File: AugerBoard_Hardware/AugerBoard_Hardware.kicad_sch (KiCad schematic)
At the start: 44 parts, among them J1 RJ45_LED_Shielded, J2 Conn_01x04_MountingPin, Q1 BSS138, Q2 BSS138, Q3 BSS138, SW1 SW_SPDT, SW2 SW_Push, SW3 SW_Push, SW4 SW_Push, U1 Teensy4.1_DEV-16771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

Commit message: Layout fun time yippie #based #awesome
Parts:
- J2: footprint Connector_PinHeader_2.54mm:PinHeader_1x04_P2.54mm_Horizontal -> Connector_PinHeader_2.54mm:PinHeader_1x04_P2.54mm_Vertical
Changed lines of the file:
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@@
 			)
 		)
-		(property "Footprint" "Connector_PinHeader_2.54mm:PinHeader_1x04_P2.54mm_Horizontal"
+		(property "Footprint" "Connector_PinHeader_2.54mm:PinHeader_1x04_P2.54mm_Vertical"
 			(at 180.34 160.02 0)
 			(effects

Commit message: Layout made smaller hai
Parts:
- Conn10, Conn11, Conn4, Conn5: footprint MRDT_Connectors:MOLEX_SL_02_Horizontal -> MRDT_Connectors:MOLEX_SL_02_Vertical
- Conn13, Conn15, Conn9: footprint MRDT_Connectors:MOLEX_SL_05_Horizontal -> MRDT_Connectors:MOLEX_SL_05_Vertical
- Conn2, Conn3: footprint MRDT_Connectors:MOLEX_SL_04_Horizontal -> MRDT_Connectors:MOLEX_SL_04_Vertical
- Conn7: footprint MRDT_Connectors:MOLEX_SL_03_Horizontal -> MRDT_Connectors:MOLEX_SL_03_Vertical
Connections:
- net +3.3V: now also U1.3.3V_1 (3.3V), U1.3.3V_2 (3.3V), U1.3.3V_3 (3.3V)
- no-connect marks 23 -> 22
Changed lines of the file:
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@@
 	)
 	(no_connect
-		(at 265.43 31.75)
-	)
-	(no_connect
 		(at 265.43 34.29)
 	)
@@
 	(wire
 		(pts
+			(xy 273.05 31.75) (xy 265.43 31.75)
+		)
+		(stroke
+			(width 0)
+			(type default)
+		)
+	)
+	(wire
+		(pts
 			(xy 127 170.18) (xy 132.08 170.18)
 		)
@@
 	(wire
 		(pts
+			(xy 273.05 26.67) (xy 273.05 31.75)
+		)
+		(stroke
+			(width 0)
+			(type default)
+		)
+	)
+	(wire
+		(pts
 			(xy 351.79 196.85) (xy 351.79 199.39)
 		)
@@
 	)
 	(symbol
+		(lib_id "power:+3.3V")
+		(at 273.05 26.67 0)
+		(unit 1)
+		(exclude_from_sim no)
+		(in_bom yes)
+		(on_board yes)
+		(dnp no)
+		(fields_autoplaced yes)
+		(property "Reference" "#PWR014"
+			(at 273.05 30.48 0)
+			(effects
+				(font
+					(size 1.27 1.27)
+				)
+				(hide yes)
+			)
+		)
+		(property "Value" "+3.3V"
+			(at 273.05 21.59 0)
+			(effects
+				(font
+					(size 1.27 1.27)
+				)
+			)
+		)
+		(property "Footprint" ""
+			(at 273.05 26.67 0)
+			(effects
+				(font
+					(size 1.27 1.27)
+				)
+				(hide yes)
+			)
+		)
+		(property "Datasheet" ""
+			(at 273.05 26.67 0)
+			(effects
+				(font
+					(size 1.27 1.27)
+				)
+				(hide yes)
+			)
+		)
+		(property "Description" "Power symbol creates a global label with name \"+3.3V\""
+			(at 273.05 26.67 0)
+			(effects
+				(font
+					(size 1.27 1.27)
+				)
+				(hide yes)
+			)
+		)
+		(pin "1"
+		)
+		(instances
+			(project ""
+				(path "/eb675789-6cce-4465-8b28-94d3d6dee9aa"
+					(reference "#PWR014")
+					(unit 1)
+				)
+			)
+		)
+	)
+	(symbol
 		(lib_id "Switch:SW_Push")
 		(at 111.76 93.98 0)
@@
 			)
 		)
-		(property "Footprint" "MRDT_Connectors:MOLEX_SL_04_Horizontal"
+		(property "Footprint" "MRDT_Connectors:MOLEX_SL_04_Vertical"
 			(at 167.64 36.83 0)
 			(effects
@@
 			)
 		)
-		(property "Footprint" "MRDT_Connectors:MOLEX_SL_02_Horizontal"
+		(property "Footprint" "MRDT_Connectors:MOLEX_SL_02_Vertical"
 			(at 67.31 132.08 0)
 			(effects
@@
 			)
 		)
-		(property "Footprint" "MRDT_Connectors:MOLEX_SL_03_Horizontal"
+		(property "Footprint" "MRDT_Connectors:MOLEX_SL_03_Vertical"
 			(at 231.14 167.64 0)
 			(effects
@@
 			)
 		)
-		(property "Footprint" "MRDT_Connectors:MOLEX_SL_04_Horizontal"
+		(property "Footprint" "MRDT_Connectors:MOLEX_SL_04_Vertical"
 			(at 167.64 59.69 0)
 			(effects
@@
 			)
 		)
-		(property "Footprint" "MRDT_Connectors:MOLEX_SL_02_Horizontal"
+		(property "Footprint" "MRDT_Connectors:MOLEX_SL_02_Vertical"
 			(at 67.31 104.14 0)
 			(effects
@@
 			)
 		)
-		(property "Footprint" "MRDT_Connectors:MOLEX_SL_05_Horizontal"
+		(property "Footprint" "MRDT_Connectors:MOLEX_SL_05_Vertical"
 			(at 387.35 118.11 0)
 			(effects
@@
 			)
 		)
-		(property "Footprint" "MRDT_Connectors:MOLEX_SL_02_Horizontal"
+		(property "Footprint" "MRDT_Connectors:MOLEX_SL_02_Vertical"
 			(at 67.31 193.04 0)
 			(effects
@@
 			)
 		)
-		(property "Footprint" "MRDT_Connectors:MOLEX_SL_05_Horizontal"
+		(property "Footprint" "MRDT_Connectors:MOLEX_SL_05_Vertical"
 			(at 386.08 229.87 0)
 			(effects
@@
 			)
 		)
-		(property "Footprint" "MRDT_Connectors:MOLEX_SL_05_Horizontal"
+		(property "Footprint" "MRDT_Connectors:MOLEX_SL_05_Vertical"
 			(at 387.35 175.26 0)
 			(effects
@@
 			)
 		)
-		(property "Footprint" "MRDT_Connectors:MOLEX_SL_02_Horizontal"
+		(property "Footprint" "MRDT_Connectors:MOLEX_SL_02_Vertical"
 			(at 67.31 162.56 0)
 			(effects

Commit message: Layout made smaller h
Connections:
- net SEL3: no longer names the net of U1.41 (A17)
- no-connect marks 22 -> 25
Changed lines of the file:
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@@
+	)
+	(no_connect
+		(at 224.79 85.09)
 	)
 	(no_connect
@@
 	)
 	(no_connect
+		(at 271.78 97.79)
+	)
+	(no_connect
 		(at 265.43 34.29)
 	)
@@
 	(no_connect
 		(at 265.43 67.31)
+	)
+	(no_connect
+		(at 224.79 92.71)
 	)
 	(no_connect
@@
 				(hide yes)
 			)
-		)
-	)
-	(global_label "SEL3"
-		(shape output)
-		(at 271.78 97.79 0)
-		(fields_autoplaced yes)
-		(effects
-			(font
-				(size 1.27 1.27)
-			)
-			(justify left)
-		)
-		(property "Intersheetrefs" "${INTERSHEET_REFS}"
-			(at 279.3613 97.79 0)
-			(effects
-				(font
-					(size 1.27 1.27)
-				)
-				(justify left)
-				(hide yes)
-			)

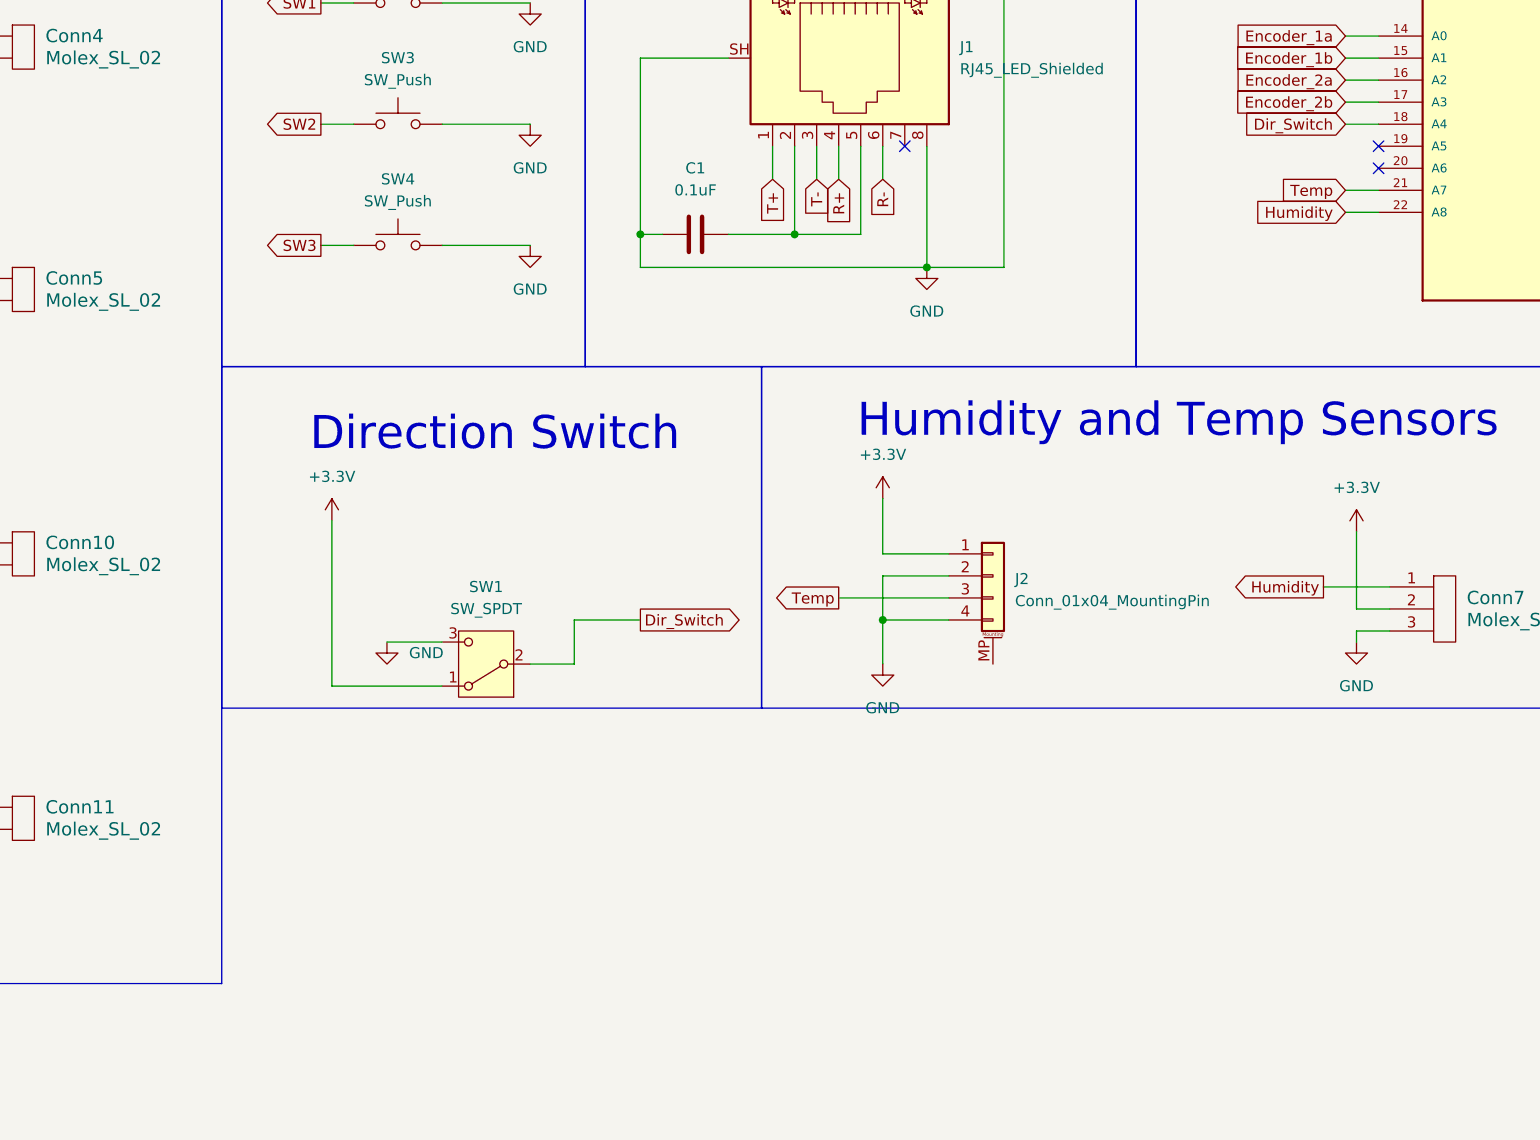
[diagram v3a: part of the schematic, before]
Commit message: Added IR sensor/emitter and rerouted shtuff
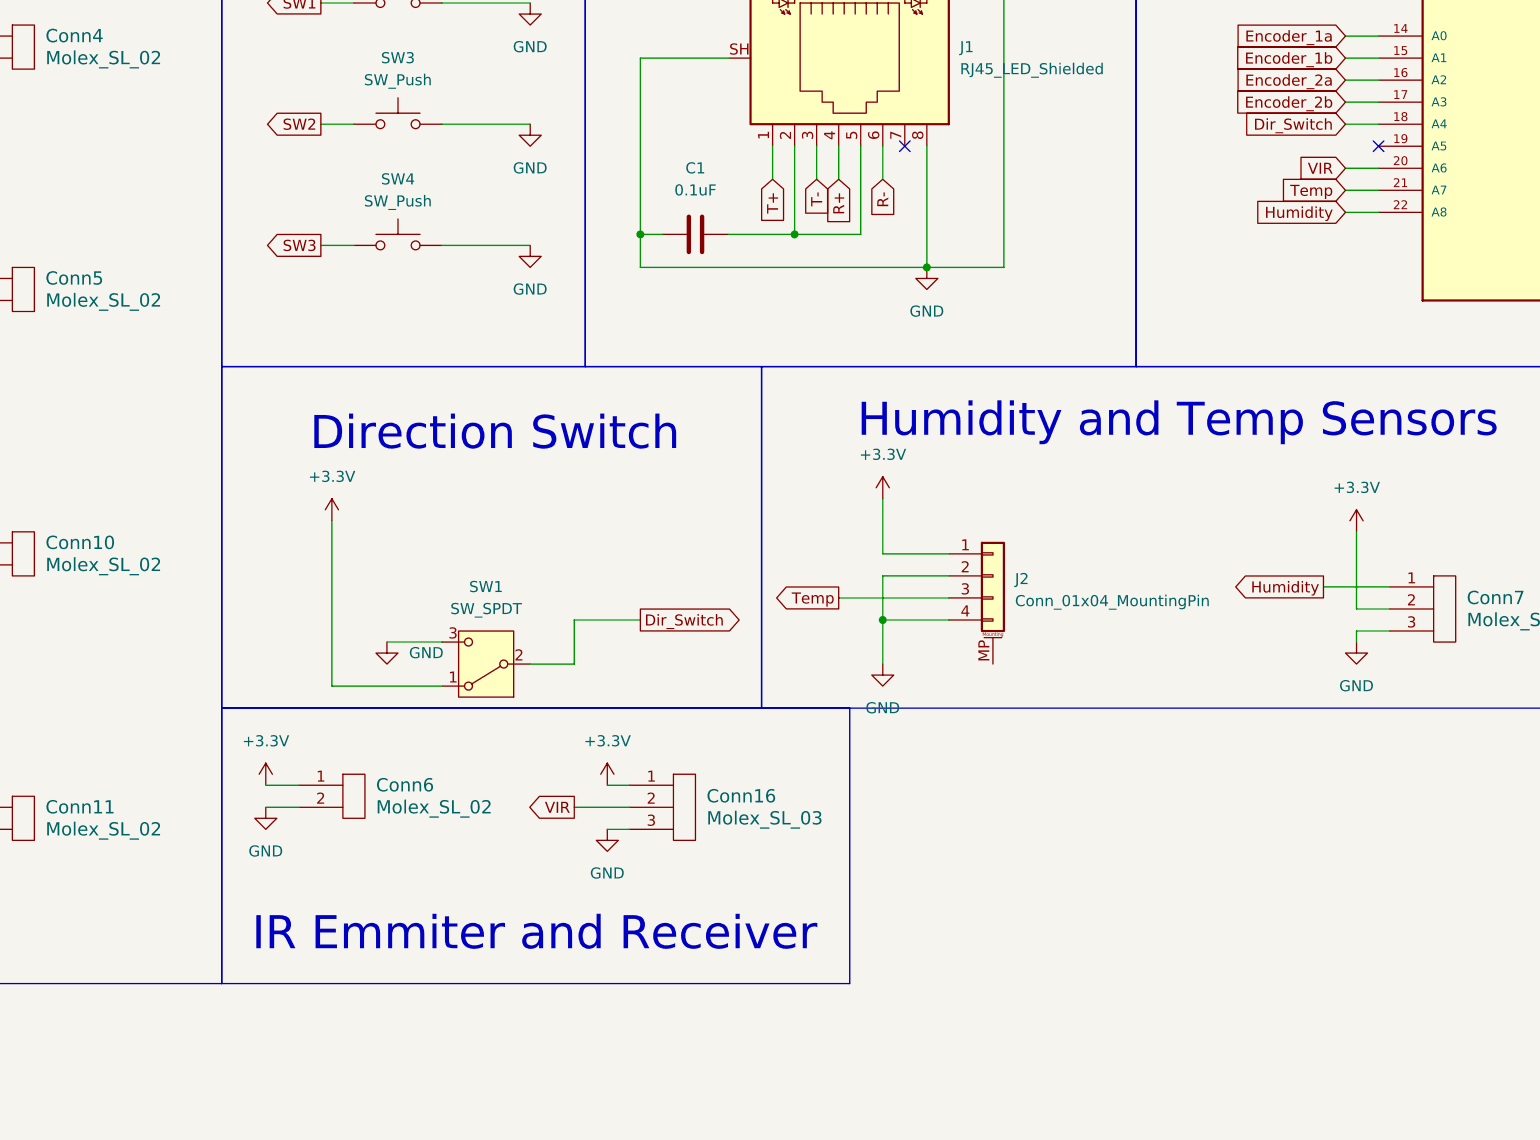
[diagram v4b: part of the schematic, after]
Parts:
- added Conn16: Molex_SL_03, MRDT_Connectors:MOLEX_SL_03_Vertical, symbol MRDT_Connectors:Molex_SL_03
- added Conn6: Molex_SL_02, MRDT_Connectors:MOLEX_SL_02_Vertical, symbol MRDT_Connectors:Molex_SL_02
- Conn1, Conn12, Conn14, Conn8: footprint MRDT_Connectors:Square_Anderson_2_H_Side_By_Side_PV -> MRDT_Connectors:Square_Anderson_2_H_Side_By_Side
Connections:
- net +3.3V: now also Conn16.1, Conn6.1
- net GND: now also Conn16.3, Conn6.2
- net VIR: now reaches U1.20 (A6)
- net VIR: now also Conn16.2
- no-connect marks 25 -> 24
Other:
- note added: "IR Emmiter and Receiver"

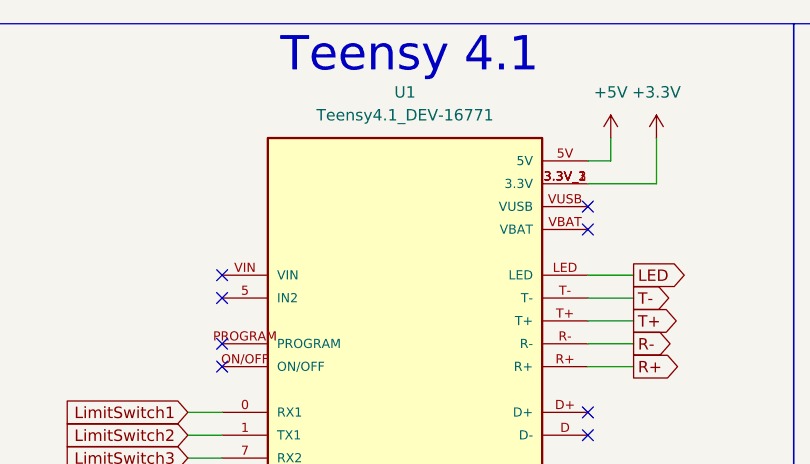
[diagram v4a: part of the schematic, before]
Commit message: 5 volt to teensy fixed (single worst trace ever made)
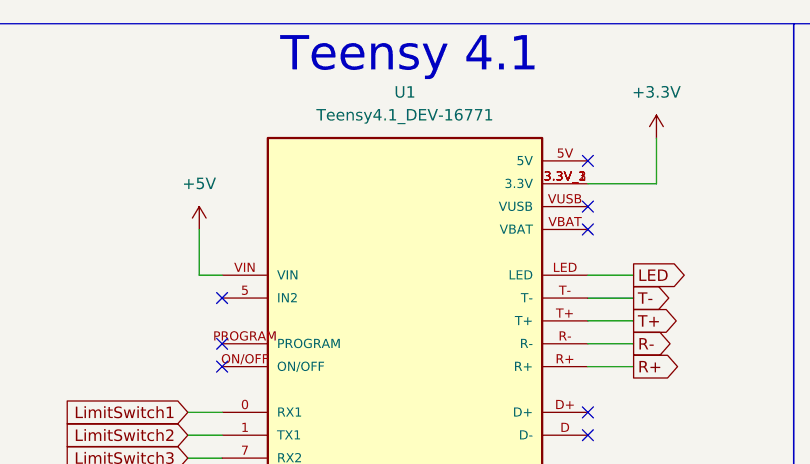
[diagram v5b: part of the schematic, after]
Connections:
- net +5V: now also U1.VIN; no longer U1.5V
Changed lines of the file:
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@@
 	)
 	(no_connect
-		(at 224.79 41.91)
-	)
-	(no_connect
 		(at 224.79 49.53)
 	)
@@
 	)
 	(no_connect
+		(at 265.43 29.21)
+	)
+	(no_connect
 		(at 154.94 90.17)
 	)
@@
 	(wire
 		(pts
+			(xy 222.25 41.91) (xy 222.25 36.83)
+		)
+		(stroke
+			(width 0)
+			(type default)
+		)
+	)
+	(wire
+		(pts
 			(xy 351.79 118.11) (xy 351.79 121.92)
 		)
@@
 	(wire
 		(pts
+			(xy 224.79 41.91) (xy 222.25 41.91)
+		)
+		(stroke
+			(width 0)
+			(type default)
+		)
+	)
+	(wire
+		(pts
 			(xy 181.61 90.17) (xy 181.61 124.46)
 		)
@@
 	(wire
 		(pts
-			(xy 265.43 29.21) (xy 267.97 29.21)
-		)
-		(stroke
-			(width 0)
-			(type default)
-		)
-	)
-	(wire
-		(pts
 			(xy 220.98 102.87) (xy 224.79 102.87)
 		)
@@
 	(wire
 		(pts
-			(xy 267.97 29.21) (xy 267.97 26.67)
-		)
-		(stroke
-			(width 0)
-			(type default)
-		)
-	)
-	(wire
-		(pts
 			(xy 219.71 69.85) (xy 224.79 69.85)
 		)
@@
 	(symbol
 		(lib_id "power:+5V")
-		(at 267.97 26.67 0)
+		(at 222.25 36.83 0)
 		(unit 1)
 		(exclude_from_sim no)
@@
 		(fields_autoplaced yes)
 		(property "Reference" "#PWR02"
-			(at 267.97 30.48 0)
+			(at 222.25 40.64 0)
 			(effects
 				(font
@@
 		)
 		(property "Value" "+5V"
-			(at 267.97 21.59 0)
+			(at 222.25 31.75 0)
 			(effects
 				(font
@@
 		)
 		(property "Footprint" ""
-			(at 267.97 26.67 0)
+			(at 222.25 36.83 0)
 			(effects
 				(font
@@
 		)
 		(property "Datasheet" ""
-			(at 267.97 26.67 0)
+			(at 222.25 36.83 0)
 			(effects
 				(font
@@
 		)
 		(property "Description" "Power symbol creates a global label with name \"+5V\""
-			(at 267.97 26.67 0)
+			(at 222.25 36.83 0)
 			(effects
 				(font
